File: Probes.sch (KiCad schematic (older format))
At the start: 11 parts, among them U3 INA333

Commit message: Assigned footprints
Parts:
- C5, C6: footprint (none) -> Capacitor_SMD:C_0805_2012Metric_Pad1.15x1.40mm_HandSolder
- C7: footprint (none) -> Capacitor_THT:CP_Axial_L18.0mm_D8.0mm_P25.00mm_Horizontal
- R1, R2, R3, R4, R5, R6, R7: footprint (none) -> Resistor_SMD:R_0805_2012Metric_Pad1.15x1.40mm_HandSolder
- U3: footprint (none) -> Package_SO:VSSOP-8_3.0x3.0mm_P0.65mm
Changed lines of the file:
@@
 F 0 "R1" V 4068 3325 50  0000 C CNN
 F 1 "1k" V 4159 3325 50  0000 C CNN
-F 2 "" V 4205 3325 50  0001 C CNN
+F 2 "Resistor_SMD:R_0805_2012Metric_Pad1.15x1.40mm_HandSolder" V 4205 3325 50  0001 C CNN
 F 3 "~" H 4275 3325 50  0001 C CNN
 	1    4275 3325
@@
 F 0 "R2" V 4068 3725 50  0000 C CNN
 F 1 "1k" V 4159 3725 50  0000 C CNN
-F 2 "" V 4205 3725 50  0001 C CNN
+F 2 "Resistor_SMD:R_0805_2012Metric_Pad1.15x1.40mm_HandSolder" V 4205 3725 50  0001 C CNN
 F 3 "~" H 4275 3725 50  0001 C CNN
 	1    4275 3725
@@
 F 0 "R4" V 4543 3725 50  0000 C CNN
 F 1 "1k" V 4634 3725 50  0000 C CNN
-F 2 "" V 4680 3725 50  0001 C CNN
+F 2 "Resistor_SMD:R_0805_2012Metric_Pad1.15x1.40mm_HandSolder" V 4680 3725 50  0001 C CNN
 F 3 "~" H 4750 3725 50  0001 C CNN
 	1    4750 3725
@@
 F 0 "R3" V 4543 3325 50  0000 C CNN
 F 1 "1k" V 4634 3325 50  0000 C CNN
-F 2 "" V 4680 3325 50  0001 C CNN
+F 2 "Resistor_SMD:R_0805_2012Metric_Pad1.15x1.40mm_HandSolder" V 4680 3325 50  0001 C CNN
 F 3 "~" H 4750 3325 50  0001 C CNN
 	1    4750 3325
@@
 F 0 "C5" V 4498 2900 50  0000 C CNN
 F 1 "47nF" V 4589 2900 50  0000 C CNN
-F 2 "" H 4788 2750 50  0001 C CNN
+F 2 "Capacitor_SMD:C_0805_2012Metric_Pad1.15x1.40mm_HandSolder" H 4788 2750 50  0001 C CNN
 F 3 "~" H 4750 2900 50  0001 C CNN
 	1    4750 2900
@@
 F 0 "C6" V 4498 4050 50  0000 C CNN
 F 1 "47nF" V 4589 4050 50  0000 C CNN
-F 2 "" H 4788 3900 50  0001 C CNN
+F 2 "Capacitor_SMD:C_0805_2012Metric_Pad1.15x1.40mm_HandSolder" H 4788 3900 50  0001 C CNN
 F 3 "~" H 4750 4050 50  0001 C CNN
 	1    4750 4050
@@
 F 0 "U3" H 5875 3975 50  0000 L CNN
 F 1 "INA333" H 6200 3975 50  0000 L CNN
-F 2 "" H 6100 3550 50  0001 C CNN
+F 2 "Package_SO:VSSOP-8_3.0x3.0mm_P0.65mm" H 6100 3550 50  0001 C CNN
 F 3 "https://www.ti.com/lit/ds/symlink/ina333.pdf" H 6100 3550 50  0001 C CNN
 	1    6100 3550
@@
 F 0 "R5" H 5545 3346 50  0000 L CNN
 F 1 "1k" H 5545 3255 50  0000 L CNN
-F 2 "" V 5405 3300 50  0001 C CNN
+F 2 "Resistor_SMD:R_0805_2012Metric_Pad1.15x1.40mm_HandSolder" V 5405 3300 50  0001 C CNN
 F 3 "~" H 5475 3300 50  0001 C CNN
 	1    5475 3300
@@
 F 0 "R6" V 3693 4125 50  0000 C CNN
 F 1 "68K" V 3784 4125 50  0000 C CNN
-F 2 "" V 3830 4125 50  0001 C CNN
+F 2 "Resistor_SMD:R_0805_2012Metric_Pad1.15x1.40mm_HandSolder" V 3830 4125 50  0001 C CNN
 F 3 "~" H 3900 4125 50  0001 C CNN
 	1    3900 4125
@@
 F 0 "C7" V 7102 3550 50  0000 C CNN
 F 1 "CP1" V 7011 3550 50  0000 C CNN
-F 2 "" H 6850 3550 50  0001 C CNN
-F 3 "~" H 6850 3550 50  0001 C CNN
+F 2 "Capacitor_THT:CP_Axial_L18.0mm_D8.0mm_P25.00mm_Horizontal" H 6850 3550 50  0001 C CNN
+F 3 "https://www.illinoiscapacitor.com/pdf/seriesDocuments/AXZ%20series.pdf" H 6850 3550 50  0001 C CNN
 	1    6850 3550
 	0    -1   -1   0
@@
 F 0 "R7" H 7320 3896 50  0000 L CNN
 F 1 "3k" H 7320 3805 50  0000 L CNN
-F 2 "" V 7180 3850 50  0001 C CNN
+F 2 "Resistor_SMD:R_0805_2012Metric_Pad1.15x1.40mm_HandSolder" V 7180 3850 50  0001 C CNN
 F 3 "~" H 7250 3850 50  0001 C CNN
 	1    7250 3850

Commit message: #2 - Add ECG input via headphone jack
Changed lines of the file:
@@
 $EndComp
 Wire Wire Line
-	3750 3325 4125 3325
-Wire Wire Line
-	3750 3725 4125 3725
+	3750 3325 4025 3325
+Wire Wire Line
+	3750 3725 4025 3725
 Wire Wire Line
 	4425 3325 4525 3325
@@
 Text HLabel 3750 4125 0    50   Input Italic 0
 P3in
+$Comp
+L power:PWR_FLAG #FLG0105
+U 1 1 5FBE4DBA
+P 4025 3325
+F 0 "#FLG0105" H 4025 3400 50  0001 C CNN
+F 1 "PWR_FLAG" H 4025 3498 50  0000 C CNN
+F 2 "" H 4025 3325 50  0001 C CNN
+F 3 "~" H 4025 3325 50  0001 C CNN
+	1    4025 3325
+	1    0    0    -1
+$EndComp
+Connection ~ 4025 3325
+Wire Wire Line
+	4025 3325 4125 3325
+$Comp
+L power:PWR_FLAG #FLG0106
+U 1 1 5FBE57AC
+P 4025 3725
+F 0 "#FLG0106" H 4025 3800 50  0001 C CNN
+F 1 "PWR_FLAG" H 4025 3898 50  0000 C CNN
+F 2 "" H 4025 3725 50  0001 C CNN
+F 3 "~" H 4025 3725 50  0001 C CNN
+	1    4025 3725
+	1    0    0    -1
+$EndComp
+Connection ~ 4025 3725
+Wire Wire Line
+	4025 3725 4125 3725
+$Comp
+L power:PWR_FLAG #FLG0107
+U 1 1 5FBE5B53
+P 3750 4125
+F 0 "#FLG0107" H 3750 4200 50  0001 C CNN
+F 1 "PWR_FLAG" H 3750 4298 50  0000 C CNN
+F 2 "" H 3750 4125 50  0001 C CNN
+F 3 "~" H 3750 4125 50  0001 C CNN
+	1    3750 4125
+	1    0    0    -1
+$EndComp
 $EndSCHEMATC

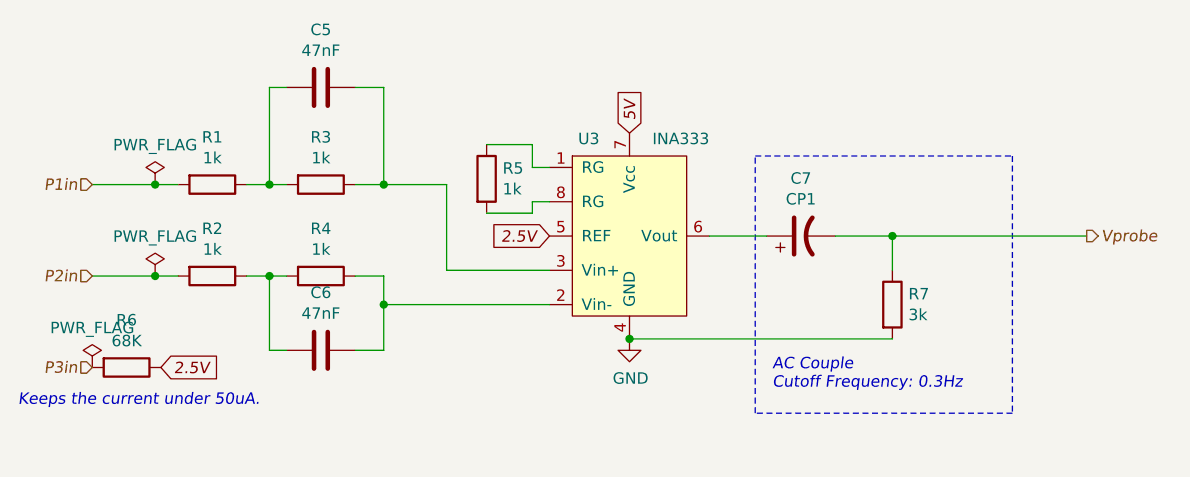
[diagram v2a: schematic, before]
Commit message: #8 - Add test points. (Also updated filter circuit)
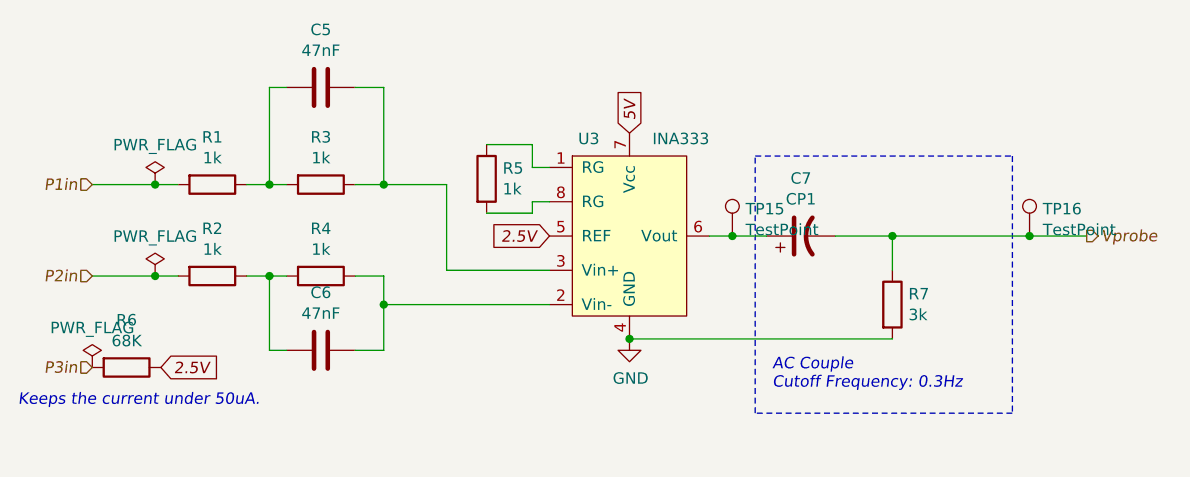
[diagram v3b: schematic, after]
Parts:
- added TP15, TP16: TestPoint, TestPoint:TestPoint_Pad_D2.0mm, symbol Connector:TestPoint
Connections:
- net Vprobe: now also TP16.1
- net at C7.1, U3.6 (Vout): now also TP15.1
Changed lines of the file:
@@
 $EndComp
 Wire Wire Line
-	6450 3550 6700 3550
+	6450 3550 6550 3550
 Wire Wire Line
 	7000 3550 7250 3550
@@
 	6650 4325 6650 3200
 Wire Wire Line
-	8100 3550 7250 3550
+	8100 3550 7850 3550
 Connection ~ 7250 3550
 Text HLabel 8100 3550 2    50   Output Italic 0
@@
 	1    0    0    -1
 $EndComp
+$Comp
+L Connector:TestPoint TP15
+U 1 1 5FC9DF1C
+P 6550 3550
+F 0 "TP15" H 6608 3668 50  0000 L CNN
+F 1 "TestPoint" H 6608 3577 50  0000 L CNN
+F 2 "TestPoint:TestPoint_Pad_D2.0mm" H 6750 3550 50  0001 C CNN
+F 3 "~" H 6750 3550 50  0001 C CNN
+	1    6550 3550
+	1    0    0    -1
+$EndComp
+Connection ~ 6550 3550
+Wire Wire Line
+	6550 3550 6700 3550
+$Comp
+L Connector:TestPoint TP16
+U 1 1 5FC9E5E5
+P 7850 3550
+F 0 "TP16" H 7908 3668 50  0000 L CNN
+F 1 "TestPoint" H 7908 3577 50  0000 L CNN
+F 2 "TestPoint:TestPoint_Pad_D2.0mm" H 8050 3550 50  0001 C CNN
+F 3 "~" H 8050 3550 50  0001 C CNN
+	1    7850 3550
+	1    0    0    -1
+$EndComp
+Connection ~ 7850 3550
+Wire Wire Line
+	7850 3550 7250 3550
 $EndSCHEMATC

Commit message: #4 - Added the heart edge cut and updated the Kicad footprints that were removed
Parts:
- C5, C6: footprint Capacitor_SMD:C_0805_2012Metric_Pad1.15x1.40mm_HandSolder -> Capacitor_SMD:C_0805_2012Metric_Pad1.18x1.45mm_HandSolder
- R1, R2, R3, R4, R5, R6, R7: footprint Resistor_SMD:R_0805_2012Metric_Pad1.15x1.40mm_HandSolder -> Resistor_SMD:R_0805_2012Metric_Pad1.20x1.40mm_HandSolder
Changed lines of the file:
@@
 F 0 "R1" V 4068 3325 50  0000 C CNN
 F 1 "1k" V 4159 3325 50  0000 C CNN
-F 2 "Resistor_SMD:R_0805_2012Metric_Pad1.15x1.40mm_HandSolder" V 4205 3325 50  0001 C CNN
+F 2 "Resistor_SMD:R_0805_2012Metric_Pad1.20x1.40mm_HandSolder" V 4205 3325 50  0001 C CNN
 F 3 "~" H 4275 3325 50  0001 C CNN
 	1    4275 3325
@@
 F 0 "R2" V 4068 3725 50  0000 C CNN
 F 1 "1k" V 4159 3725 50  0000 C CNN
-F 2 "Resistor_SMD:R_0805_2012Metric_Pad1.15x1.40mm_HandSolder" V 4205 3725 50  0001 C CNN
+F 2 "Resistor_SMD:R_0805_2012Metric_Pad1.20x1.40mm_HandSolder" V 4205 3725 50  0001 C CNN
 F 3 "~" H 4275 3725 50  0001 C CNN
 	1    4275 3725
@@
 F 0 "R4" V 4543 3725 50  0000 C CNN
 F 1 "1k" V 4634 3725 50  0000 C CNN
-F 2 "Resistor_SMD:R_0805_2012Metric_Pad1.15x1.40mm_HandSolder" V 4680 3725 50  0001 C CNN
+F 2 "Resistor_SMD:R_0805_2012Metric_Pad1.20x1.40mm_HandSolder" V 4680 3725 50  0001 C CNN
 F 3 "~" H 4750 3725 50  0001 C CNN
 	1    4750 3725
@@
 F 0 "R3" V 4543 3325 50  0000 C CNN
 F 1 "1k" V 4634 3325 50  0000 C CNN
-F 2 "Resistor_SMD:R_0805_2012Metric_Pad1.15x1.40mm_HandSolder" V 4680 3325 50  0001 C CNN
+F 2 "Resistor_SMD:R_0805_2012Metric_Pad1.20x1.40mm_HandSolder" V 4680 3325 50  0001 C CNN
 F 3 "~" H 4750 3325 50  0001 C CNN
 	1    4750 3325
@@
 F 0 "C5" V 4498 2900 50  0000 C CNN
 F 1 "47nF" V 4589 2900 50  0000 C CNN
-F 2 "Capacitor_SMD:C_0805_2012Metric_Pad1.15x1.40mm_HandSolder" H 4788 2750 50  0001 C CNN
+F 2 "Capacitor_SMD:C_0805_2012Metric_Pad1.18x1.45mm_HandSolder" H 4788 2750 50  0001 C CNN
 F 3 "~" H 4750 2900 50  0001 C CNN
 	1    4750 2900
@@
 F 0 "C6" V 4498 4050 50  0000 C CNN
 F 1 "47nF" V 4589 4050 50  0000 C CNN
-F 2 "Capacitor_SMD:C_0805_2012Metric_Pad1.15x1.40mm_HandSolder" H 4788 3900 50  0001 C CNN
+F 2 "Capacitor_SMD:C_0805_2012Metric_Pad1.18x1.45mm_HandSolder" H 4788 3900 50  0001 C CNN
 F 3 "~" H 4750 4050 50  0001 C CNN
 	1    4750 4050
@@
 F 0 "R5" H 5545 3346 50  0000 L CNN
 F 1 "1k" H 5545 3255 50  0000 L CNN
-F 2 "Resistor_SMD:R_0805_2012Metric_Pad1.15x1.40mm_HandSolder" V 5405 3300 50  0001 C CNN
+F 2 "Resistor_SMD:R_0805_2012Metric_Pad1.20x1.40mm_HandSolder" V 5405 3300 50  0001 C CNN
 F 3 "~" H 5475 3300 50  0001 C CNN
 	1    5475 3300
@@
 F 0 "R6" V 3693 4125 50  0000 C CNN
 F 1 "68K" V 3784 4125 50  0000 C CNN
-F 2 "Resistor_SMD:R_0805_2012Metric_Pad1.15x1.40mm_HandSolder" V 3830 4125 50  0001 C CNN
+F 2 "Resistor_SMD:R_0805_2012Metric_Pad1.20x1.40mm_HandSolder" V 3830 4125 50  0001 C CNN
 F 3 "~" H 3900 4125 50  0001 C CNN
 	1    3900 4125
@@
 F 0 "R7" H 7320 3896 50  0000 L CNN
 F 1 "3k" H 7320 3805 50  0000 L CNN
-F 2 "Resistor_SMD:R_0805_2012Metric_Pad1.15x1.40mm_HandSolder" V 7180 3850 50  0001 C CNN
+F 2 "Resistor_SMD:R_0805_2012Metric_Pad1.20x1.40mm_HandSolder" V 7180 3850 50  0001 C CNN
 F 3 "~" H 7250 3850 50  0001 C CNN
 	1    7250 3850

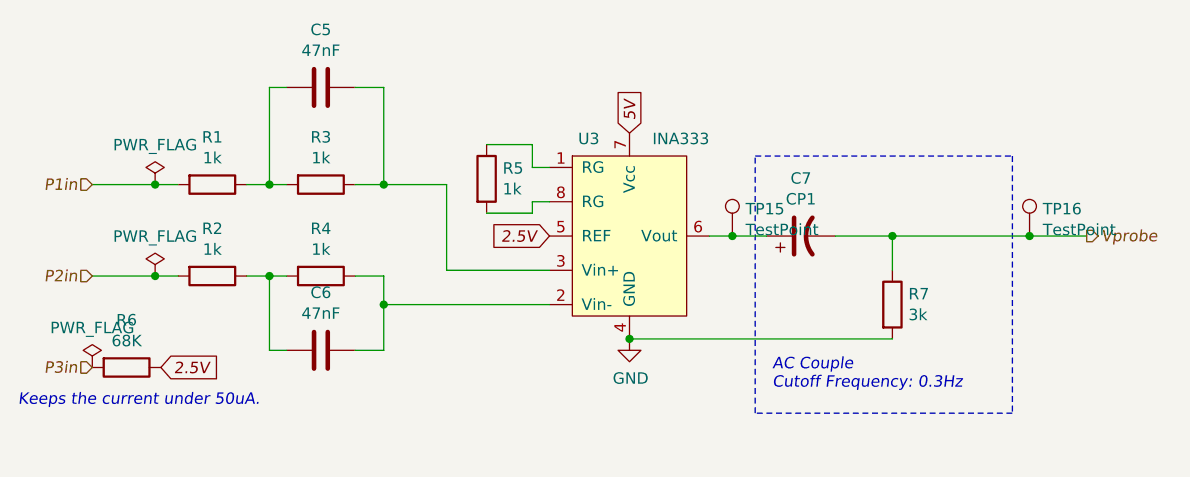
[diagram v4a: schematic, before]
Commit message: Added bypass caps on ICs and fixed the SHDN input.
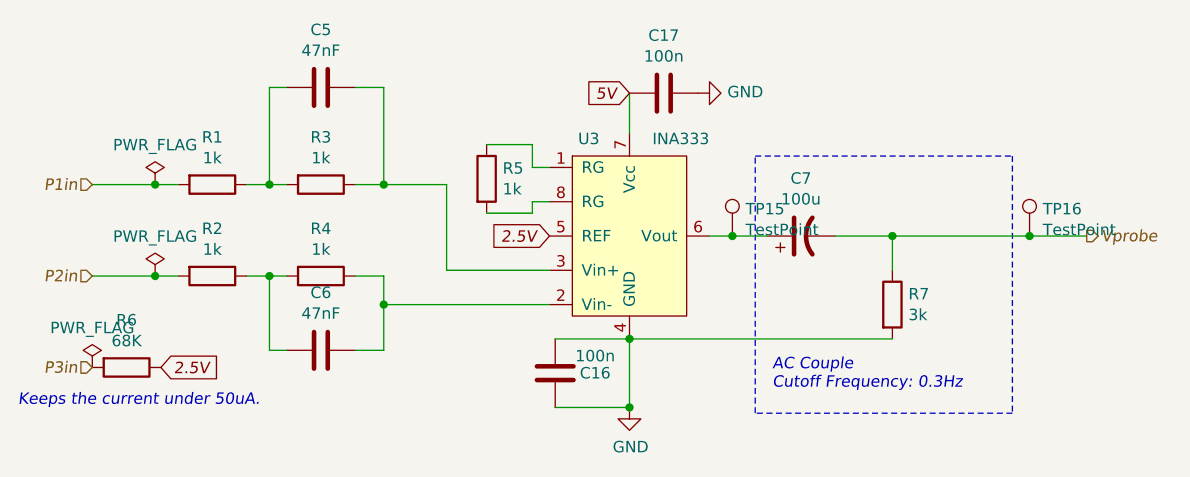
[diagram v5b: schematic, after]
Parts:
- added C16, C17: 100n, Capacitor_SMD:C_0805_2012Metric_Pad1.18x1.45mm_HandSolder, symbol Device:C
- C7: value CP1 -> 100u
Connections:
- net 5V: now also C17.2
- net GND: now also C16.1, C16.2, C17.1
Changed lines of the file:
@@
 L power:GND #PWR01
 U 1 1 5FA062F9
-P 6100 4000
-F 0 "#PWR01" H 6100 3750 50  0001 C CNN
-F 1 "GND" H 6105 3827 50  0000 C CNN
-F 2 "" H 6100 4000 50  0001 C CNN
-F 3 "" H 6100 4000 50  0001 C CNN
-	1    6100 4000
+P 6100 4300
+F 0 "#PWR01" H 6100 4050 50  0001 C CNN
+F 1 "GND" H 6105 4127 50  0000 C CNN
+F 2 "" H 6100 4300 50  0001 C CNN
+F 3 "" H 6100 4300 50  0001 C CNN
+	1    6100 4300
 	1    0    0    -1
 $EndComp
-Text GLabel 6100 3100 1    50   Input Italic 0
+Text GLabel 6100 2925 0    50   Input Italic 0
 5V
 $Comp
@@
 P 6850 3550
 F 0 "C7" V 7102 3550 50  0000 C CNN
-F 1 "CP1" V 7011 3550 50  0000 C CNN
+F 1 "100u" V 7011 3550 50  0000 C CNN
 F 2 "Capacitor_THT:CP_Axial_L18.0mm_D8.0mm_P25.00mm_Horizontal" H 6850 3550 50  0001 C CNN
 F 3 "https://www.illinoiscapacitor.com/pdf/seriesDocuments/AXZ%20series.pdf" H 6850 3550 50  0001 C CNN
@@
 Wire Wire Line
 	7850 3550 7250 3550
+$Comp
+L Device:C C17
+U 1 1 5FCAEA62
+P 6250 2925
+F 0 "C17" V 5998 2925 50  0000 C CNN
+F 1 "100n" V 6089 2925 50  0000 C CNN
+F 2 "Capacitor_SMD:C_0805_2012Metric_Pad1.18x1.45mm_HandSolder" H 6288 2775 50  0001 C CNN
+F 3 "~" H 6250 2925 50  0001 C CNN
+	1    6250 2925
+	0    1    1    0
+$EndComp
+$Comp
+L power:GND #PWR018
+U 1 1 5FCB2A52
+P 6400 2925
+F 0 "#PWR018" H 6400 2675 50  0001 C CNN
+F 1 "GND" V 6405 2797 50  0000 R CNN
+F 2 "" H 6400 2925 50  0001 C CNN
+F 3 "" H 6400 2925 50  0001 C CNN
+	1    6400 2925
+	0    -1   -1   0
+$EndComp
+Wire Wire Line
+	6100 2925 6100 3100
+$Comp
+L Device:C C16
+U 1 1 5FCB8FF4
+P 5775 4150
+F 0 "C16" H 5950 4150 50  0000 C CNN
+F 1 "100n" H 5950 4225 50  0000 C CNN
+F 2 "Capacitor_SMD:C_0805_2012Metric_Pad1.18x1.45mm_HandSolder" H 5813 4000 50  0001 C CNN
+F 3 "~" H 5775 4150 50  0001 C CNN
+	1    5775 4150
+	1    0    0    -1
+$EndComp
+Wire Wire Line
+	6100 4000 5775 4000
+Wire Wire Line
+	5775 4300 6100 4300
+Connection ~ 6100 4300
+Wire Wire Line
+	6100 4000 6100 4300
 $EndSCHEMATC

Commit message: Removed extra caps and removed the tantalum cap as it was too large
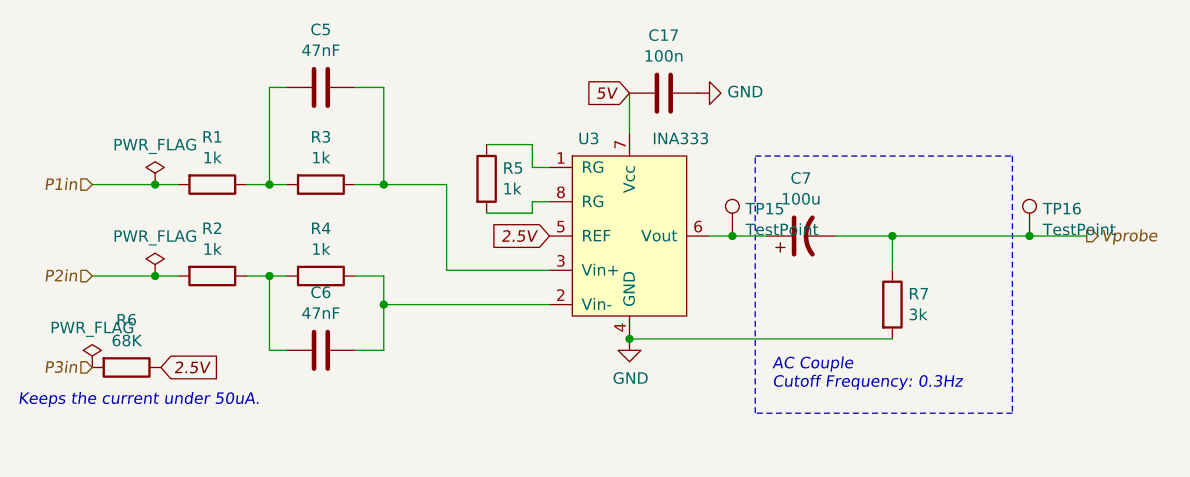
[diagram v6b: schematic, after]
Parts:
- removed C16: 100n, Capacitor_SMD:C_0805_2012Metric_Pad1.18x1.45mm_HandSolder, symbol Device:C
- C7: footprint Capacitor_THT:CP_Axial_L18.0mm_D8.0mm_P25.00mm_Horizontal -> Capacitor_SMD:C_1210_3225Metric_Pad1.33x2.70mm_HandSolder
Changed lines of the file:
@@
 L power:GND #PWR01
 U 1 1 5FA062F9
-P 6100 4300
-F 0 "#PWR01" H 6100 4050 50  0001 C CNN
-F 1 "GND" H 6105 4127 50  0000 C CNN
-F 2 "" H 6100 4300 50  0001 C CNN
-F 3 "" H 6100 4300 50  0001 C CNN
-	1    6100 4300
+P 6100 4000
+F 0 "#PWR01" H 6100 3750 50  0001 C CNN
+F 1 "GND" H 6105 3827 50  0000 C CNN
+F 2 "" H 6100 4000 50  0001 C CNN
+F 3 "" H 6100 4000 50  0001 C CNN
+	1    6100 4000
 	1    0    0    -1
 $EndComp
@@
 F 0 "C7" V 7102 3550 50  0000 C CNN
 F 1 "100u" V 7011 3550 50  0000 C CNN
-F 2 "Capacitor_THT:CP_Axial_L18.0mm_D8.0mm_P25.00mm_Horizontal" H 6850 3550 50  0001 C CNN
+F 2 "Capacitor_SMD:C_1210_3225Metric_Pad1.33x2.70mm_HandSolder" H 6850 3550 50  0001 C CNN
 F 3 "https://www.illinoiscapacitor.com/pdf/seriesDocuments/AXZ%20series.pdf" H 6850 3550 50  0001 C CNN
 	1    6850 3550
@@
 Wire Wire Line
 	7250 4000 6100 4000
-Connection ~ 6100 4000
 Text Notes 6725 4225 0    50   Italic 0
 AC Couple\nCutoff Frequency: 0.3Hz
@@
 Wire Wire Line
 	6100 2925 6100 3100
-$Comp
-L Device:C C16
-U 1 1 5FCB8FF4
-P 5775 4150
-F 0 "C16" H 5950 4150 50  0000 C CNN
-F 1 "100n" H 5950 4225 50  0000 C CNN
-F 2 "Capacitor_SMD:C_0805_2012Metric_Pad1.18x1.45mm_HandSolder" H 5813 4000 50  0001 C CNN
-F 3 "~" H 5775 4150 50  0001 C CNN
-	1    5775 4150
-	1    0    0    -1
-$EndComp
-Wire Wire Line
-	6100 4000 5775 4000
-Wire Wire Line
-	5775 4300 6100 4300
-Connection ~ 6100 4300
-Wire Wire Line
-	6100 4000 6100 4300
+Connection ~ 6100 4000
 $EndSCHEMATC
